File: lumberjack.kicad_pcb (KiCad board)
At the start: 2 copper layers, 285.4 x 94.9 mm, 156 parts, among them J1 USB, J2 AVR_ISP_6, J3 JST, SW1 RESET, SW2 BOOT, U1 ATMEGA328-PU, Y1 16MHz

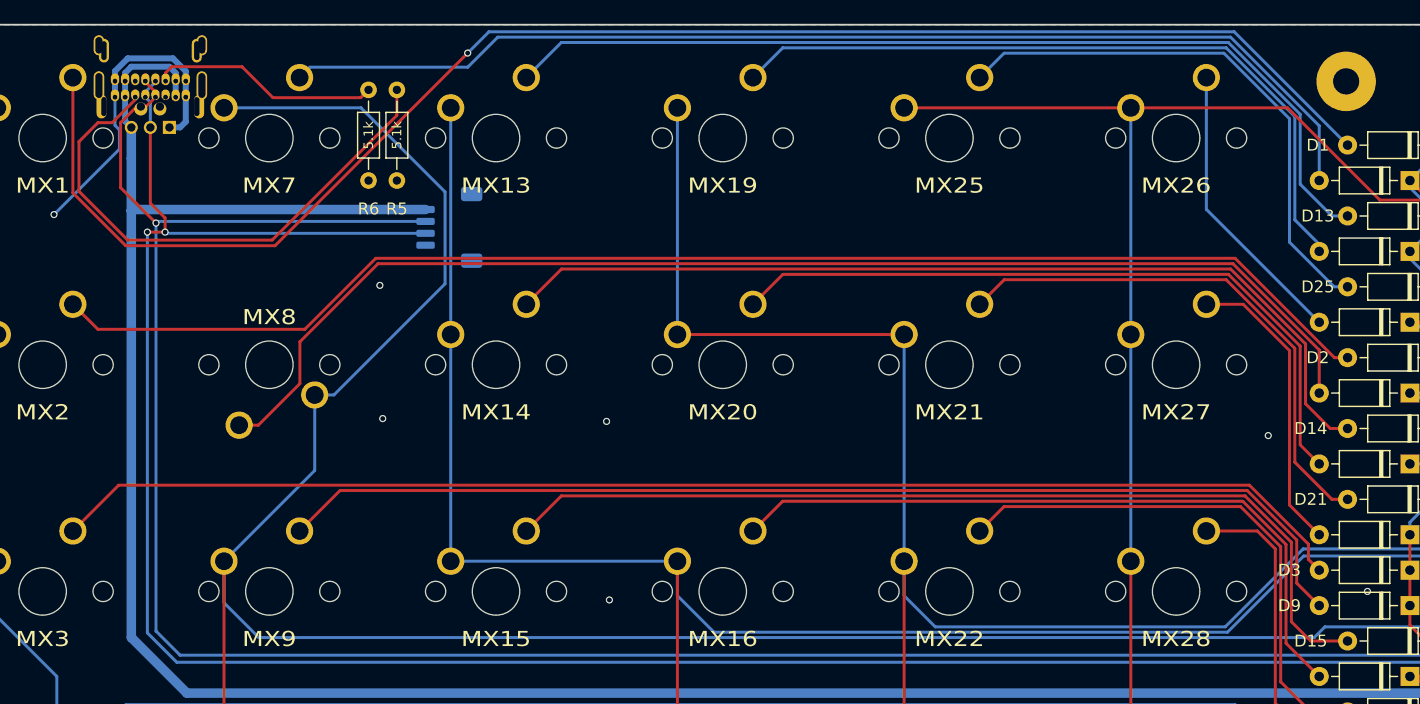
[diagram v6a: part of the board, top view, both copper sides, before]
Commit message: Move 5.1k resistors to better location
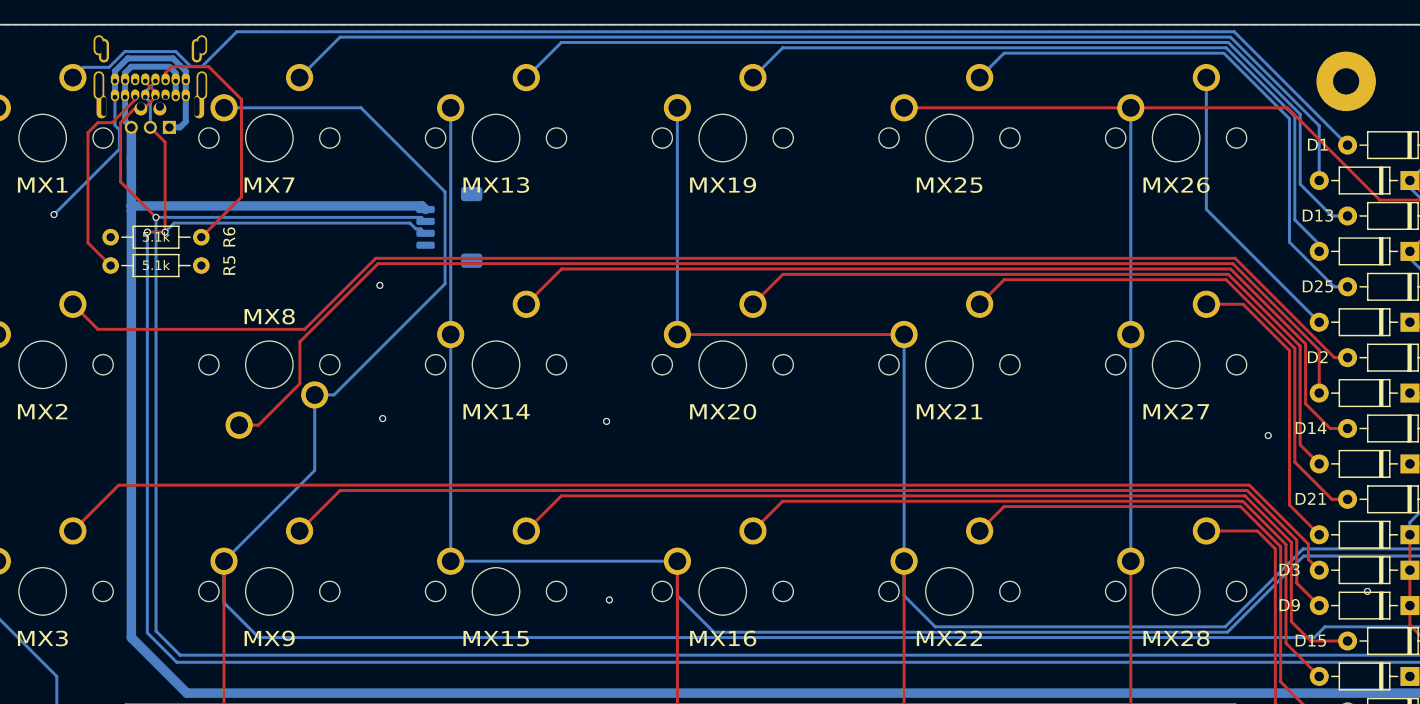
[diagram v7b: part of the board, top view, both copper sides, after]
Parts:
- moved R6 22.2 mm to (24.8, 72.6), turned to 0 degrees
- moved R5 17.9 mm to (32.4, 75.0), turned to 180 degrees
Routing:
- net Net-(J1-PadCC1): track 46.0 -> 17.8 mm
- net Net-(D1-Pad2): track 130.0 -> 113.7 mm, vias 1 -> 0
- net Net-(J1-PadCC2): track 19.3 -> 21.4 mm
- net Net-(D66-Pad1): track 211.2 -> 211.9 mm

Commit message: Change MX8 to allow both north and south facing switch
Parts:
- MX8: footprint lumberjack:MX -> lumberjack:MX_NTHSTH
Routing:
- net /COL1: track 246.9 -> 258.1 mm
- net Net-(D8-Pad2): track 105.1 -> 108.2 mm
- net Net-(D2-Pad2): track 113.9 -> 112.2 mm
- net Net-(D36-Pad2): track 116.4 -> 115.5 mm
